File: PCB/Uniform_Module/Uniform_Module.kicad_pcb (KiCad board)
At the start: 2 copper layers, 33 x 16 mm, 17 parts, among them J1 PCIE_x1_Conn_01x36_Male, SW1 Button_SMD_PTS_647_SN50_SMTR2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, SW2 Button_SMD_PTS_647_SN50_SMTR2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, U1 STM32L072KZT6

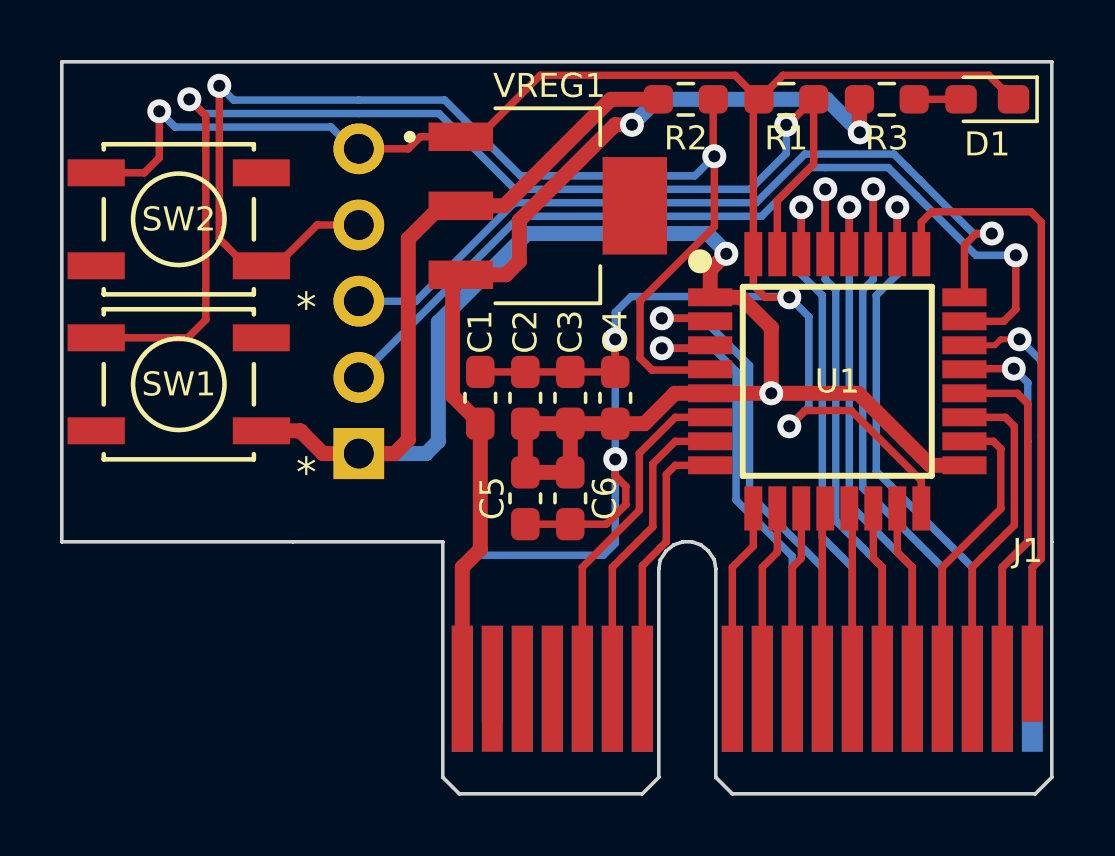
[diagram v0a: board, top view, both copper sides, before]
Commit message: silkscreen work and minor tweaks to uniform module board
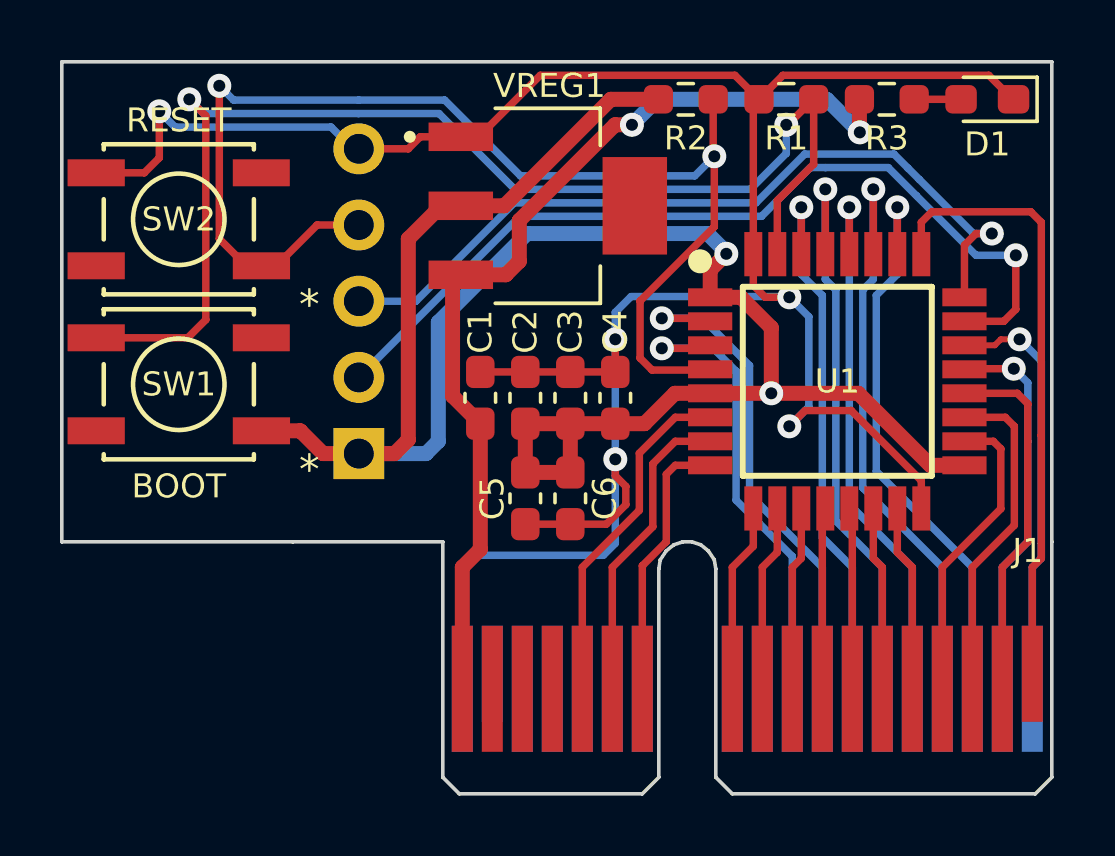
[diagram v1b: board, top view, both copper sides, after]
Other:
- board text added: "BOOT"
- board text added: "RESET"
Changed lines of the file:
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@@
       (effects (font (size 1 1) (thickness 0.15)))
     )
-    (fp_text user "*" (at -4.25 -2.95 unlocked) (layer "F.SilkS")
+    (fp_text user "*" (at -4.35 -2.85 unlocked) (layer "F.SilkS")
       (effects (font (size 1 1) (thickness 0.15)))
     )
@@
       (effects (font (size 1 1) (thickness 0.15)))
     )
-    (fp_text user "*" (at -4.25 -2.95) (layer "F.SilkS")
+    (fp_text user "*" (at -4.35 -2.85) (layer "F.SilkS")
       (effects (font (size 1 1) (thickness 0.15)))
     )
@@
     (property "Sheetname" "")
     (attr through_hole)
-    (fp_text reference "SWD1" (at -2.4 -9.81 90) (layer "B.SilkS")
+    (fp_text reference "SWD1" (at 0 2.14) (layer "B.SilkS")
       (effects (font (size 0.8 0.8) (thickness 0.15)) (justify mirror))
     )
@@
     (effects (font (size 1 1) (thickness 0.15)) (justify mirror))
   )
+  (gr_text "RESET" (at 203.315 137.01) (layer "F.SilkS")
+    (effects (font (size 0.8 0.8) (thickness 0.15)))
+  )
+  (gr_text "BOOT" (at 203.315 149.21) (layer "F.SilkS")
+    (effects (font (size 0.8 0.8) (thickness 0.15)))
+  )
   (segment (start 224.19048 146.68452) (end 223.665 147.21) (width 0.25) (layer "F.Cu") (net 1))
